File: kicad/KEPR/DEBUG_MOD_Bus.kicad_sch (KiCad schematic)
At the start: 0 parts

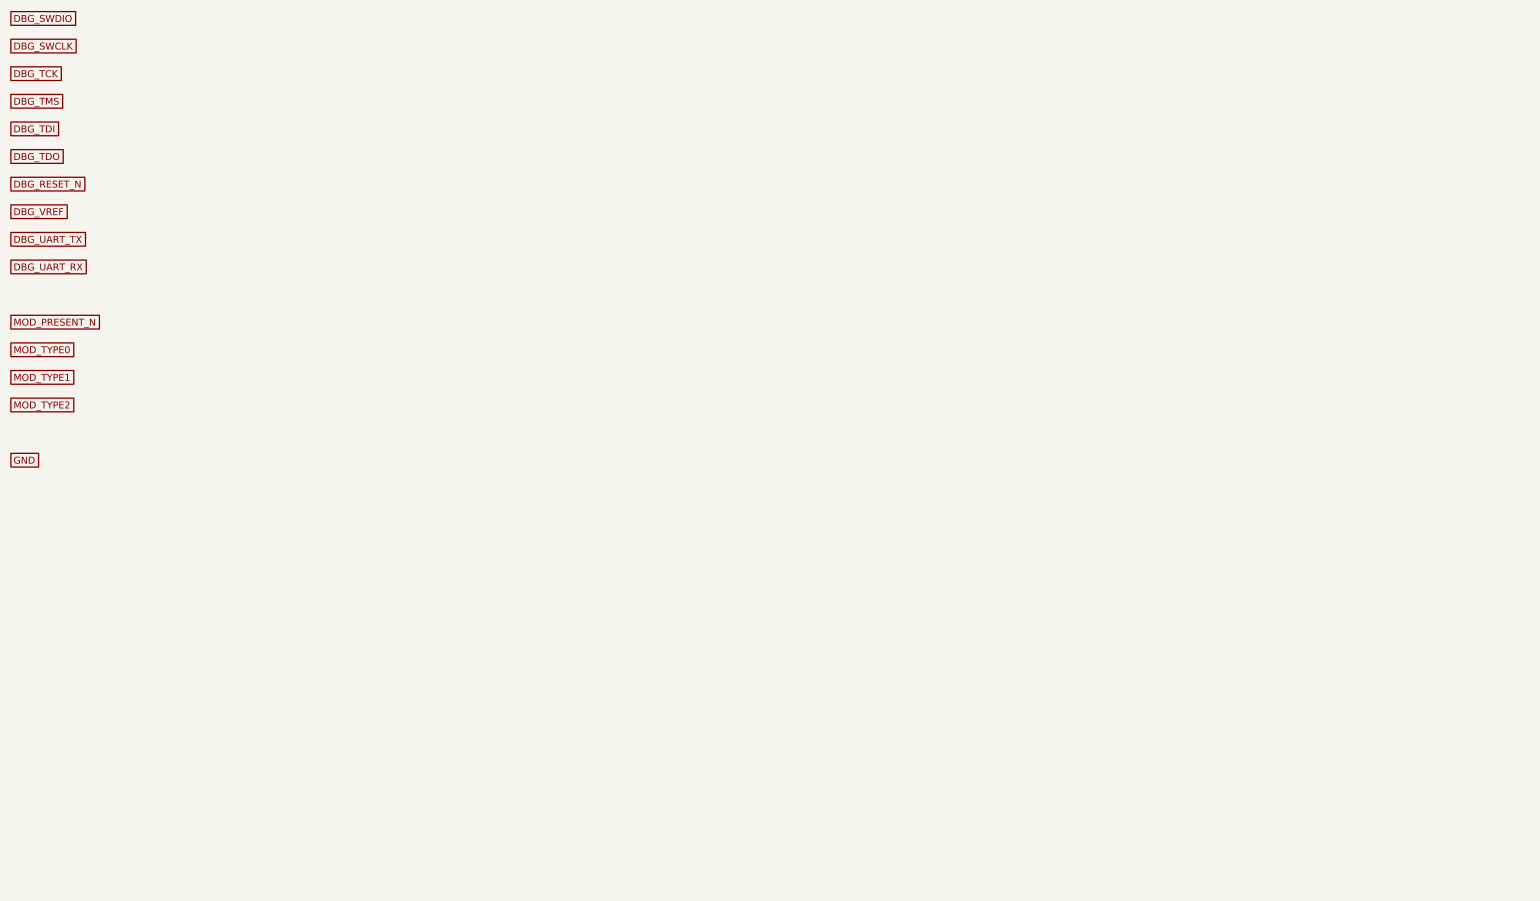
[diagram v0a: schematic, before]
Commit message: Definido os demais buses, criado folha do carimbo, versão 0.5
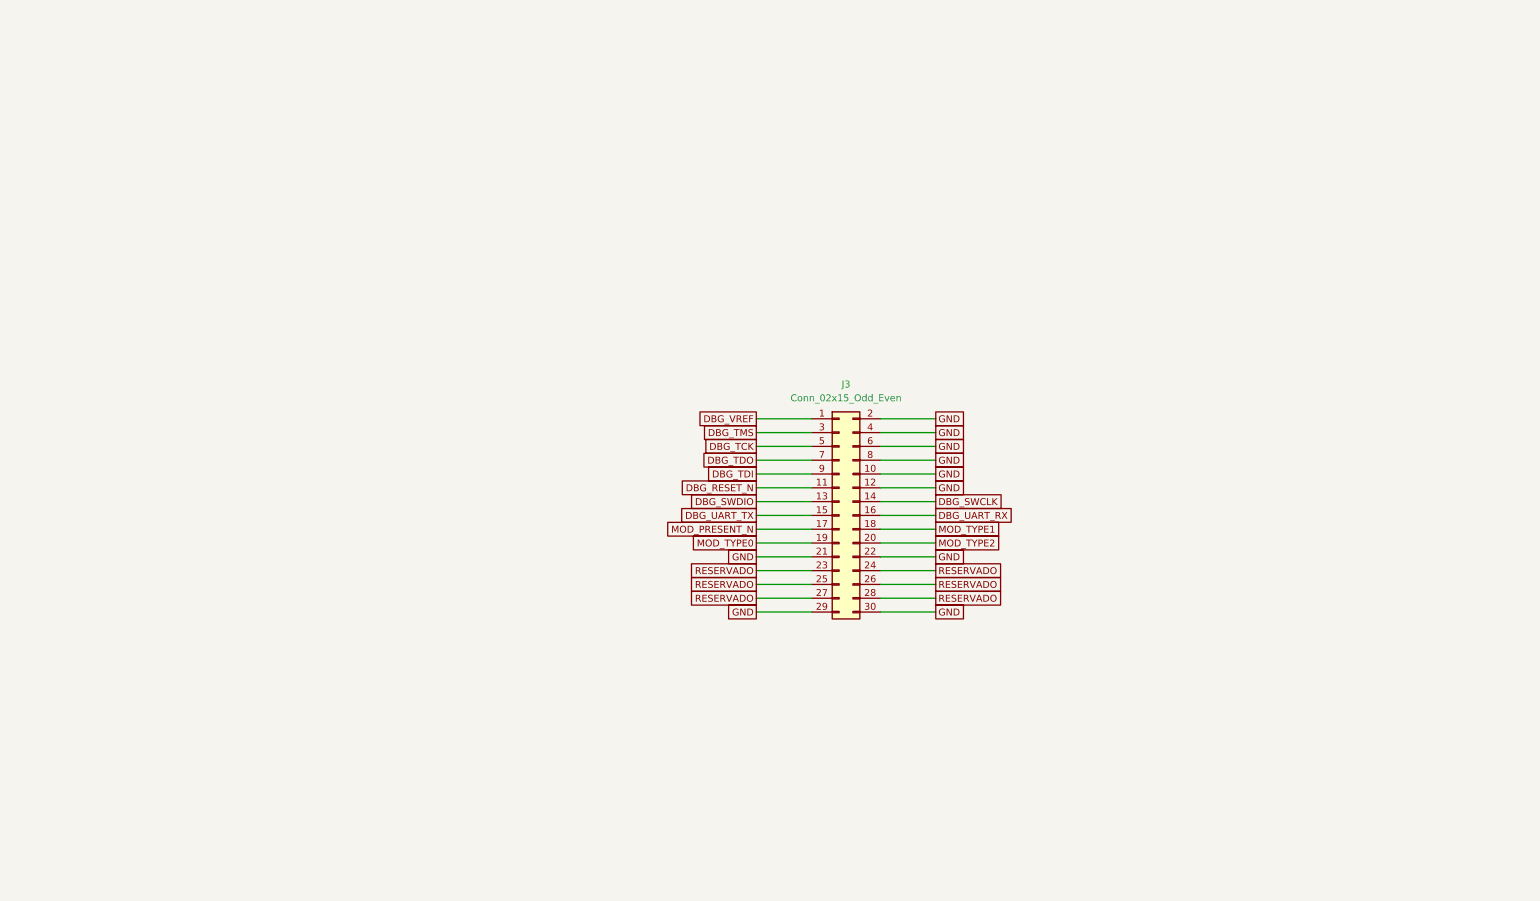
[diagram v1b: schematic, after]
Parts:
- added J3: Conn_02x15_Odd_Even, symbol Connector_Generic:Conn_02x15_Odd_Even
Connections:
- net DBG_RESET_N: now also J3.11 (Pin_11)
- net DBG_SWCLK: now also J3.14 (Pin_14)
- net DBG_SWDIO: now also J3.13 (Pin_13)
- net DBG_TCK: now also J3.5 (Pin_5)
- net DBG_TDI: now also J3.9 (Pin_9)
- net DBG_TDO: now also J3.7 (Pin_7)
- net DBG_TMS: now also J3.3 (Pin_3)
- net DBG_UART_RX: now also J3.16 (Pin_16)
- net DBG_UART_TX: now also J3.15 (Pin_15)
- net DBG_VREF: now also J3.1 (Pin_1)
- net GND: now also J3.10 (Pin_10), J3.12 (Pin_12), J3.2 (Pin_2), J3.21 (Pin_21), J3.22 (Pin_22), J3.29 (Pin_29), J3.30 (Pin_30), J3.4 (Pin_4), J3.6 (Pin_6), J3.8 (Pin_8)
- net MOD_PRESENT_N: now also J3.17 (Pin_17)
- net MOD_TYPE0: now also J3.19 (Pin_19)
- net MOD_TYPE1: now also J3.18 (Pin_18)
- net MOD_TYPE2: now also J3.20 (Pin_20)
- new net RESERVADO: J3.23 (Pin_23), J3.24 (Pin_24), J3.25 (Pin_25), J3.26 (Pin_26), J3.27 (Pin_27), J3.28 (Pin_28)

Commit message: Adicinado o barramento externo
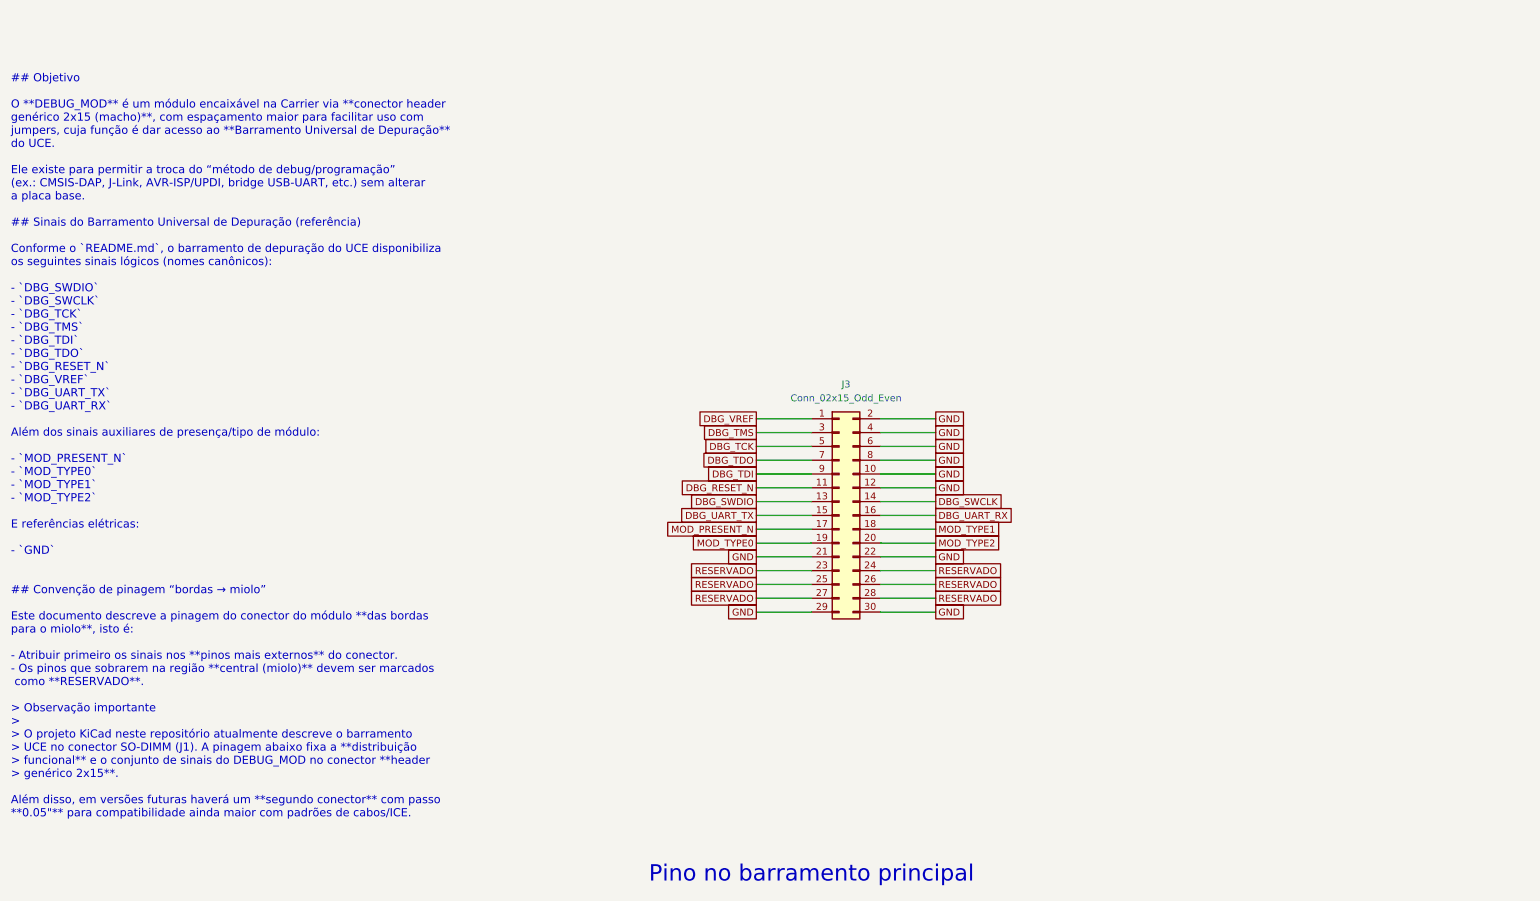
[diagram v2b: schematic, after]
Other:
- note added: "## Objetivo O **DEBUG_MOD** é um módulo encaixável na Carrier via **conector header genérico 2x15 (macho)**, com espaçamento maior para facilitar uso com jumpers, cuja função é dar acesso ao **Barramento Universal de Depuração** do UCE. Ele existe para permitir a troca do “método de debug/programação” (ex.: CMSIS-DAP, J-Link, AVR-ISP/UPDI, bridge USB-UART, etc.) sem alterar a placa base. ## Sinai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"
- note added: "Pino no barramento principal"

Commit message: Iniciado projeto da PCB, para uma referência de tamanho.
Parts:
- J4: renamed from J3; footprint (none) -> Connector_IDC:IDC-Header_2x15-1MP_P2.54mm_Latch_Vertical
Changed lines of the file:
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@@
 		(on_board yes)
 		(dnp no)
-		(fields_autoplaced yes)
-		(property "Reference" "J?"
+		(property "Reference" "J4"
 			(at 204.47 118.11 0)
 			(effects
@@
 			)
 		)
-		(property "Footprint" ""
-			(at 203.2 142.24 0)
+		(property "Footprint" "Connector_IDC:IDC-Header_2x15-1MP_P2.54mm_Latch_Vertical"
+			(at 205.74 114.3 0)
 			(effects
 				(font
 					(size 1.27 1.27)
 				)
-				(hide yes)
 			)
 		)
@@
 			(project "KEPR"
 				(path "/5d9e1dfb-5ec5-4e06-bbdb-9cbfa1c0b9f1/0260e008-78ae-4c2c-85f8-b31739d2ea08/32d5f829-b169-471c-a009-0492c35731ba"
-					(reference "J?")
+					(reference "J4")
 					(unit 1)
 				)

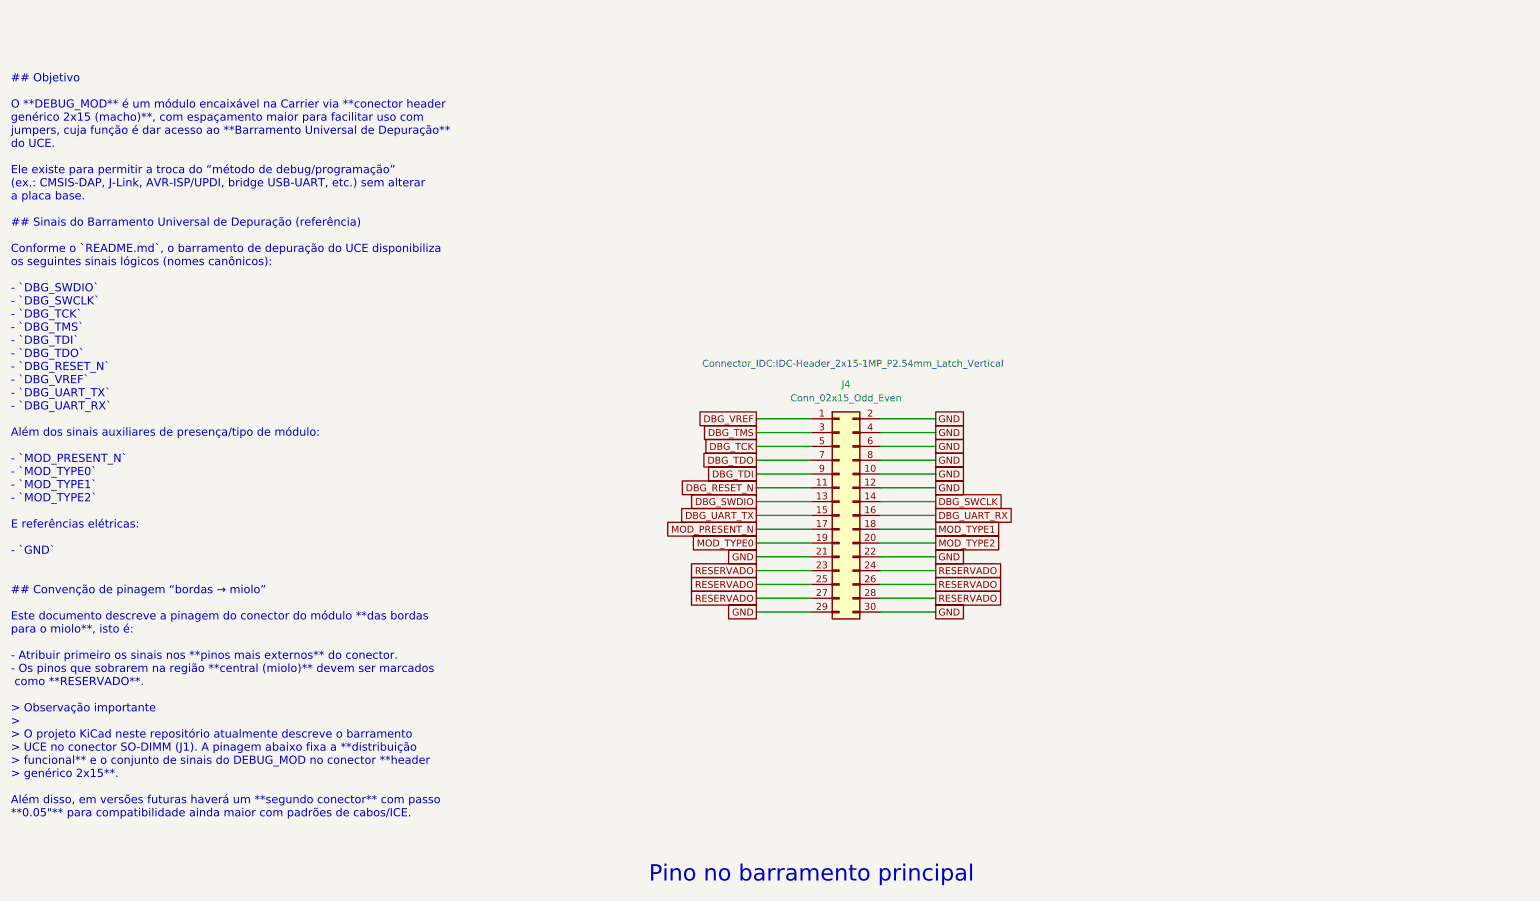
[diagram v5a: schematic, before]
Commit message: Iniciado a distribuição das vias.
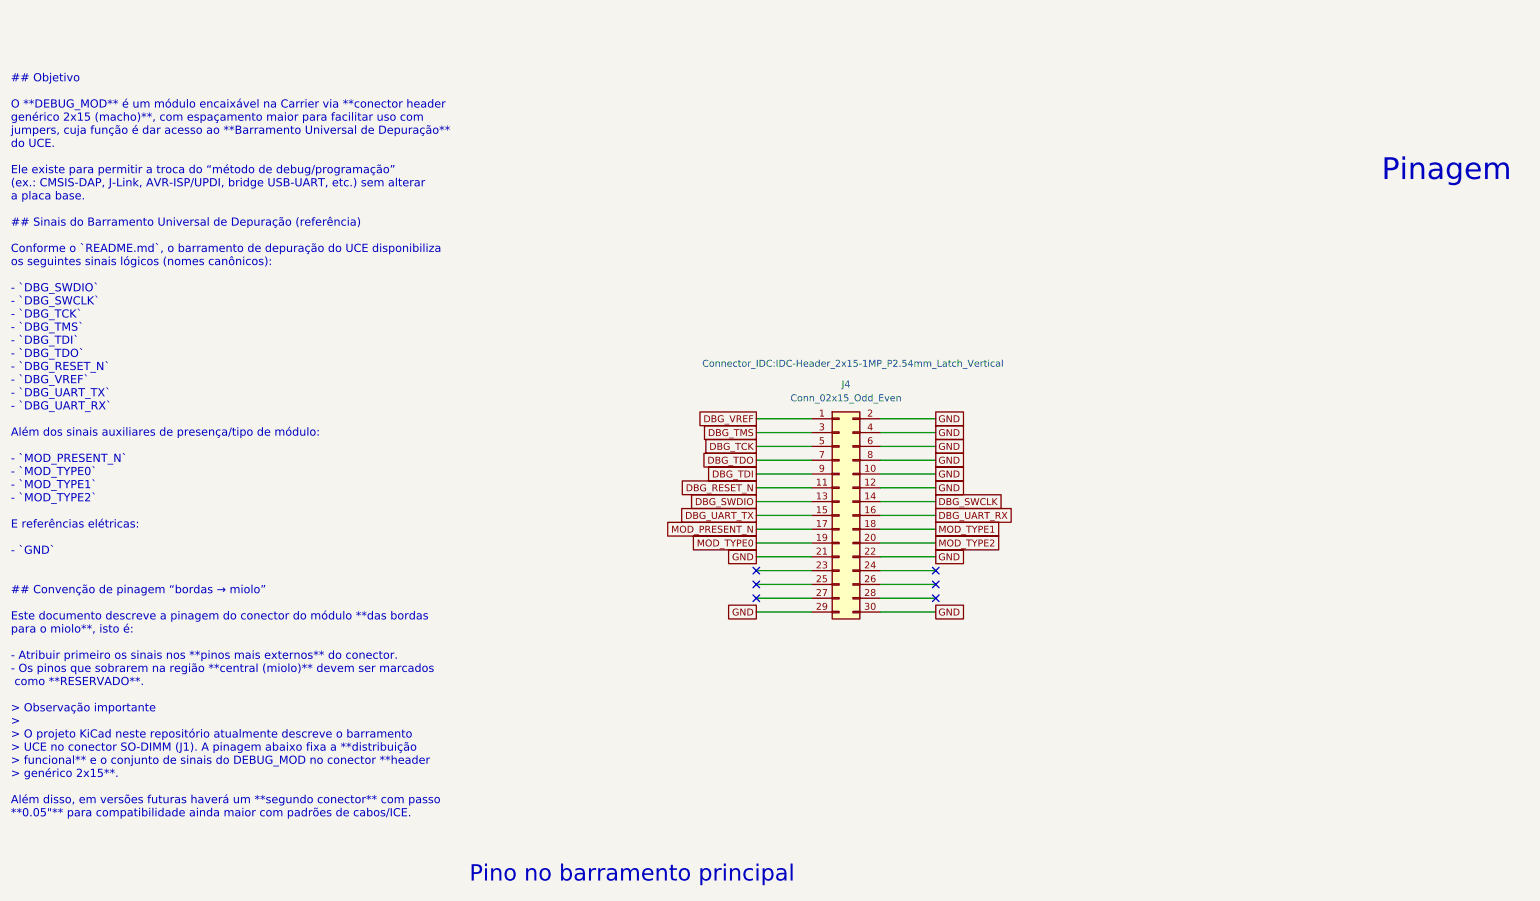
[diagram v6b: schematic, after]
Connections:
- removed net RESERVADO: J4.23 (Pin_23), J4.24 (Pin_24), J4.25 (Pin_25), J4.26 (Pin_26), J4.27 (Pin_27), J4.28 (Pin_28)
- no-connect marks 0 -> 6
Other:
- note added: "Pinagem"
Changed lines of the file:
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@@
 		(comment 7 "Carlos Delfino Carvalho Pinheiro")
+	)
+	(text "Pinagem"
+		(exclude_from_sim no)
+		(at 314.96 78.74 0)
+		(effects
+			(font
+				(size 4 4)
+			)
+		)
 	)
 	(text "Pino no barramento principal"
 		(exclude_from_sim no)
-		(at 198.12 208.28 0)
+		(at 165.1 208.28 0)
 		(effects
 			(font
@@
 			(justify left)
 		)
+	)
+	(no_connect
+		(at 187.96 154.94)
+	)
+	(no_connect
+		(at 187.96 152.4)
+	)
+	(no_connect
+		(at 187.96 157.48)
+	)
+	(no_connect
+		(at 220.98 157.48)
+	)
+	(no_connect
+		(at 220.98 154.94)
+	)
+	(no_connect
+		(at 220.98 152.4)
 	)
 	(wire
@@
 	)
 	(image
-		(at 200.66 248.92)
+		(at 167.64 248.92)
 		(scale 2.67888)
 		(data "iVBORw0KGgoAAAANSUhEUgAAAbAAAAFDCAIAAADUKszKAAAAA3NCSVQICAjb4U/gAAAgAElEQVR4"
@@
 		)
 	)
-	(global_label "RESERVADO"
-		(shape passive)
-		(at 220.98 154.94 0)
-		(effects
-			(font
-				(size 1.27 1.27)
-			)
-			(justify left bottom)
-		)
-		(property "Intersheetrefs" "${INTERSHEET_REFS}"
-			(at 220.98 154.94 0)
-			(effects
-				(font
-					(size 1.27 1.27)
-				)
-				(justify left)
-				(hide yes)
-			)
-		)
-	)
 	(global_label "GND"
 		(shape passive)
@@
 		)
 	)
-	(global_label "RESERVADO"
-		(shape passive)
-		(at 187.96 154.94 180)
-		(effects
-			(font
-				(size 1.27 1.27)
-			)
-			(justify right bottom)
-		)
-		(property "Intersheetrefs" "${INTERSHEET_REFS}"
-			(at 187.96 154.94 0)
-			(effects
-				(font
-					(size 1.27 1.27)
-				)
-				(justify right)
-				(hide yes)
-			)
-		)
-	)
-	(global_label "RESERVADO"
-		(shape passive)
-		(at 187.96 152.4 180)
-		(effects
-			(font
-				(size 1.27 1.27)
-			)
-			(justify right bottom)
-		)
-		(property "Intersheetrefs" "${INTERSHEET_REFS}"
-			(at 187.96 152.4 0)
-			(effects
-				(font
-					(size 1.27 1.27)
-				)
-				(justify right)
-				(hide yes)
-			)
-		)
-	)
-	(global_label "RESERVADO"
-		(shape passive)
-		(at 220.98 157.48 0)
-		(effects
-			(font
-				(size 1.27 1.27)
-			)
-			(justify left bottom)
-		)
-		(property "Intersheetrefs" "${INTERSHEET_REFS}"
-			(at 220.98 157.48 0)
-			(effects
-				(font
-					(size 1.27 1.27)
-				)
-				(justify left)
-				(hide yes)
-			)
-		)
-	)
 	(global_label "DBG_TMS"
 		(shape passive)
@@
 		)
 	)
-	(global_label "RESERVADO"
-		(shape passive)
-		(at 187.96 157.48 180)
-		(effects
-			(font
-				(size 1.27 1.27)
-			)
-			(justify right bottom)
-		)
-		(property "Intersheetrefs" "${INTERSHEET_REFS}"
-			(at 187.96 157.48 0)
-			(effects
-				(font
-					(size 1.27 1.27)
-				)
-				(justify right)
-				(hide yes)
-			)
-		)
-	)
 	(global_label "DBG_RESET_N"
 		(shape passive)
@@
 				(hide yes)
 			)
-		)
-	)
-	(global_label "RESERVADO"
-		(shape passive)
-		(at 220.98 152.4 0)
-		(effects
-			(font
-				(size 1.27 1.27)
-			)
-			(justify left bottom)
-		)
-		(property "Intersheetrefs" "${INTERSHEET_REFS}"
-			(at 220.98 152.4 0)
-			(effects
-				(font
-					(size 1.27 1.27)
-				)
-				(justify left)
-				(hide yes)
-			)
